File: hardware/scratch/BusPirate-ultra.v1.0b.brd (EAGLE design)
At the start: 100 x 50 mm, 177 parts, among them IC1 23LC1024, IC10 SN74LVC1T45DBV, IC11 SN74LVC1T45DBV, IC12 74LVC1G07DBV, IC13 SN74LVC1T45DBV, IC17 74LVC1G07DBV, IC18 SN74LVC1T45DBV, IC19 74LVC1G07DBV, IC2 23LC1024, IC20 SN74LVC1T45DBV, IC21 74LVC1G07DBV, IC22 SN74LVC1T45DBV, IC23 MCP1824_ADJ, IC24 74HCT4051, IC3 74AC573, IC4 74LVC1G07DBV, IC5 74LVC1G07DBV, IC6 74LVC1G07DBV, IC7 74LVC1G07DBV, IC8 SN74LVC1T45DBV, IC9 SN74LVC1T45DBV, J2 CON_HEADER_1X04, J4 CON_HEADER_1X10-RIGHT_ANGLED_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, Q1 DMMT3906W, U1 W25X40CL, U2 STM32F103ZX, U3 ICE40HX4K, U4 MCP6001, U5 MCP4442, U6 MCP4442, U7 MCP6001

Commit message: below are the changes in the schematic -remove extra pull-down resistor on VREGEN -BOOT0 and BOOT1 now connect directly to GND -change latch nets naming scheme -add divider resistors to sense voltage to Vout/Vref -renamed the control pins of the rest of the buffers -move UART to USART1 (PA9 and PA10) -connect digital pot to ARM's I2C1 (PB6 and PB7) with their pull-ups resistors, A0 and A1 wired to (PE5 and PE6) -all ADC Mux control lines are controlled only by FPGA -flip the order of latch connection of FPGA
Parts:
- added R52: 10K, dp_devices.v6:R603
- R4: device dp_devices:R603 -> dp_devices.v6:R603
- R7, R8: device rcl:R0603 -> resistor:R0603
- moved R8 273.5 mm to (-10.8, -231.8), turned to 0 degrees
- moved R7 266.4 mm to (-10.8, -226.7), turned to 0 degrees
- moved R49 241.1 mm to (-10.8, -237.5), turned to 0 degrees
- moved R4 35.1 mm to (8.89, 2.79), turned to 180 degrees
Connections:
- net ADC5 renamed MCU_ADC5
- net LAT_AUX0 renamed LAT3
- net LAT_AUX1 renamed LAT2
- net LAT_AUX2 renamed LAT1
- net LAT_AUX3 renamed LAT0
- net LAT_CLOCK renamed LAT6
- net LAT_CS renamed LAT4
- net LAT_MISO renamed LAT5
- net LAT_MOSI renamed LAT7
- removed net BOOT0: R8.1, U2.138
- removed net BOOT1: R7.1, U2.48
- removed net BUFDIR_AUX1: IC18.5, R35.2
- removed net BUFDIR_AUX2: IC20.5, R38.2
- removed net BUFDIR_AUX3: IC22.5, R41.2
- removed net BUFIO_AUX1: IC18.3
- removed net BUFIO_AUX2: IC20.3
- removed net BUFIO_AUX3: IC22.3
- removed net BUFOD_AUX1: IC17.2, R34.1
- removed net BUFOD_AUX2: IC19.2, R37.1
- removed net BUFOD_AUX3: IC21.2, R40.1
- removed net N$31: U5.11
- removed net N$33: U5.3
- removed net N$45: U2.102
- removed net N$46: U2.101
- removed net N$49: U5.4
- removed net N$50: U5.5
- removed net N$51: U6.11
- removed net N$55: U6.3
- removed net N$62: U6.4
- removed net N$63: U6.5
- new net BUFDIR5: IC18.5, R35.2, U3.88
- new net BUFDIR6: IC20.5, R38.2, U3.61
- new net BUFDIR7: IC22.5, R41.2, U3.64
- new net BUFIO5: IC18.3, U3.87
- new net BUFIO6: IC20.3, U3.60
- new net BUFIO7: IC22.3, U3.63
- new net BUFOD5: IC17.2, R34.1, U3.85
- new net BUFOD6: IC19.2, R37.1, U3.56
- new net BUFOD7: IC21.2, R40.1, U3.62
- new net MCU_ADC6: R7.2, R8.2, U2.36
- new net MCU_I2C_A0: U2.4, U5.3, U6.3
- new net MCU_I2C_A1: U2.5, U5.11, U6.11
- new net MCU_I2C_SCL: R49.1, U2.136, U5.4, U6.4
- new net MCU_I2C_SDA: R52.1, U2.137, U5.5, U6.5
- net 3V3: now also R49.2, R52.2
- net ADC_MUX_S0: no longer U2.87
- net ADC_MUX_S1: no longer U2.88
- net ADC_MUX_S2: no longer U2.89
- net BPIO0: now also IC3.9; no longer IC3.2
- net BPIO1: now also IC3.8; no longer IC3.3
- net BPIO2: now also IC3.7; no longer IC3.4
- net BPIO3: now also IC3.6; no longer IC3.5
- net BPIO4: now also IC3.5; no longer IC3.6
- net BPIO5: now also IC3.4; no longer IC3.7
- net BPIO6: now also IC3.3; no longer IC3.8
- net BPIO7: now also IC3.2; no longer IC3.9
- net GND: now also R8.1, U2.138, U2.48; no longer R49.2, R7.2, R8.2
- net N$29: now also U2.116; no longer U2.36
- net UART_RX: now also U2.102; no longer U2.137
- net UART_TX: now also U2.101; no longer U2.136
- net VREF/VOUT: now also R7.1
- net VREGEN: no longer R49.1
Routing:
- net BOOT1: track 39.3 -> 0.00 mm, vias 2 -> 0
- net 3V3: track 501.6 -> 482.6 mm
- net BOOT0: track 13.0 -> 0.00 mm
- net UART_TX: track 11.7 -> 0.00 mm
- net MCU_I2C_SCL: track 0.00 -> 11.7 mm
- net BPIO2: track 22.5 -> 33.5 mm
- net BPIO5: track 31.2 -> 20.2 mm
- net GND: track 19.3 -> 30.0 mm
- net UART_RX: track 8.41 -> 0.00 mm
- net MCU_I2C_SDA: track 0.00 -> 8.41 mm
- net BPIO7: track 19.3 -> 13.2 mm
- net BPIO0: track 20.2 -> 24.3 mm
- net BPIO6: track 13.1 -> 10.6 mm
- net VREGEN: track 85.8 -> 85.1 mm

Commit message: fix digital pots address lines voltage reg DAC buffer opamp (MCP6001), shorted the feedback, change R45 value to 100K, remove C62, added devider resistors R47(78.7K) and R46(50K), removed input resistor R48, add input cap initial change to small package (SC-70, 0402) IO-0 buffer
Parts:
- removed C62: 0.1uF, dp_devices.v6:C603
- removed R48: 1M, dp_devices.v6:R603
- added C53: (no value), dp_devices.v6:C603
- C39, C45: device rcl:C0603 -> rcl:C0402
- IC4: device 74xx-little-de:SOT23-5 -> dp_devices.v6:SC-70-5
- IC8: device dp_devices.v6:DBV-R-PDSO-G6 -> dp_devices.v6:SC-70-6
- R19, R24, R28: device rcl:R0603 -> rcl:R0402
- R45: value 330R -> 100K
- R46: value (none) -> 50K
- R47: value (none) -> 78.7K
- moved R28 1.55 mm to (81.7, 14.5), turned to 90 degrees
- moved C39 1.27 mm to (79.4, 17.1)
- moved R24 1.27 mm to (81.3, 12.1)
- moved R19 1.02 mm to (77.5, 12.1)
- moved C45 0.76 mm to (81.7, 17.8)
- moved IC8 0.76 mm to (79.4, 15.1)
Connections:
- removed net ADC3: U2.41
- removed net ADC4: U2.40
- removed net MCU_I2C_A0: U2.4, U5.3, U6.3
- removed net MCU_I2C_A1: U2.5, U5.11, U6.11
- removed net N$15: R46.2, R47.1, U4.3
- removed net VREG_PWM: R48.2
- new net VREG_DAC: C53.1, U2.40, U4.3
- net 3V3: now also U6.3
- net GND: now also C53.2, R46.2, U5.11, U5.3, U6.11; no longer C62.2, R47.2
- net N$12: now also R47.2; no longer U4.1
- net N$25: now also R47.1, U4.1; no longer C62.1, R48.1
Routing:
- net N$15: track 3.87 -> 0.00 mm
- net N$25: track 3.72 -> 0.00 mm
- net BPIO0: track 24.3 -> 21.1 mm
- net N$12: track 10.4 -> 9.35 mm
- net 3V3: track 482.6 -> 483.6 mm
- net BUFIO0: track 17.3 -> 18.0 mm
- net GND: vias 138 -> 136

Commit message: place 0R resistor on the feedback of vreg DAC buffer and placed an rc filter on the input. replace with 10uF cap on the adj vreg chip input. change buffer chip with an SC-70 packages and 0402 caps and resitors
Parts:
- added R48: (no value), dp_devices.v6:R603
- added R53: 0R, dp_devices.v6:R603
- C40, C41, C42, C43, C46, C47, C48, C49: device rcl:C0603 -> resistor:C0402
- C63: value 0.1uF -> 10uF
- IC10, IC11, IC13, IC18, IC20, IC22, IC9: device dp_devices.v6:DBV-R-PDSO-G6 -> dp_devices.v6:SC-70-6
- IC12, IC17, IC19, IC21, IC5, IC6, IC7: device 74xx-little-de:SOT23-5 -> dp_devices.v6:SC-70-5
- R19, R24, R28: device rcl:R0402 -> resistor:R0402
- R20, R21, R22, R23, R25, R26, R27, R29, R30, R31, R32, R33, R40: device rcl:R0603 -> resistor:R0402
- moved R41 122.7 mm to (64.1, 3.81), turned to 90 degrees
- moved C59 118.3 mm to (58.4, 7.62), turned to 90 degrees
- moved C60 117.9 mm to (64.1, 7.62), turned to 90 degrees
- moved R42 117.2 mm to (64.1, 1.27)
- moved IC22 113.1 mm to (61.0, 7.62), turned to 90 degrees
- moved R38 109.6 mm to (73.7, 3.81), turned to 90 degrees
- moved R40 108.0 mm to (58.4, 3.79), turned to 90 degrees
- moved R39 104.0 mm to (73.7, 1.91)
- moved C58 103.9 mm to (73.7, 7.62), turned to 90 degrees
- moved R35 103.7 mm to (83.2, 5.08)
- moved C57 103.5 mm to (66.7, 7.62), turned to 90 degrees
- moved IC21 103.4 mm to (61.0, 3.17)
- moved IC20 100.5 mm to (70.5, 7.62), turned to 90 degrees
- moved R36 97.7 mm to (83.2, 3.17)
- moved C56 97.1 mm to (83.2, 8.26)
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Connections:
- new net N$15: R53.1, U4.4
- new net N$31: C53.1, R48.2, U4.3
- net N$25: now also R53.2; no longer U4.4
- net VREG_DAC: now also R48.1; no longer C53.1, U4.3
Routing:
- net ADC1: track 57.3 -> 47.1 mm
- net BUFOD3: track 9.98 -> 18.0 mm
- net VREF/VOUT: track 173.7 -> 168.0 mm
- net BUFDIR2: track 21.6 -> 26.3 mm
- net BUFOD4: track 18.0 -> 14.4 mm
- net BUFDIR4: track 22.5 -> 25.3 mm
- net BPIO0: track 21.1 -> 18.4 mm
- net BPIO3: track 40.0 -> 37.5 mm
- net 3V3: track 483.6 -> 485.8 mm
- net BUFDIR1: track 10.4 -> 8.50 mm
- net BPIO1: track 28.0 -> 26.7 mm
- net BUFOD1: track 9.75 -> 8.92 mm
- net BUFDIR3: track 15.5 -> 16.2 mm
- net BUFOD2: track 15.1 -> 15.6 mm
- net GND: vias 136 -> 134

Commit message: latch's OE tied to gnd, move things around
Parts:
- C55, C56, C57, C58, C59, C60: device rcl:C0603 -> resistor:C0402
- IC10, IC11, IC13, IC18, IC20, IC22, IC8, IC9: device dp_devices.v6:SC-70-6 -> dp_devices.v6:SC-70-6_EXTENDED_PADS
- IC12, IC17, IC19, IC21, IC4, IC5, IC6, IC7: device dp_devices.v6:SC-70-5 -> dp_devices.v6:SC-70-5_EXTENDED_PADS
- R34, R35, R36, R37, R38, R39, R41, R42: device rcl:R0603 -> resistor:R0402
- moved R52 288.8 mm to (15.2, 44.5)
- moved R49 285.0 mm to (15.2, 46.4)
- moved R53 269.6 mm to (12.7, 10.2)
- moved R48 263.6 mm to (8.26, 10.2)
- moved C53 258.5 mm to (8.26, 8.89)
- moved R8 244.1 mm to (29.8, 8.89)
- moved R51 241.4 mm to (70.5, 4.45)
- moved R7 238.4 mm to (26.0, 8.89)
- moved C51 238.2 mm to (69.8, 6.35)
- moved C14 232.4 mm to (66.7, 6.35)
- moved C44 230.2 mm to (84.5, 46.4), turned to 180 degrees
- moved TP8 229.0 mm to (10.8, 36.2)
- moved D1 226.8 mm to (66.7, 4.45)
- moved TP7 226.5 mm to (10.8, 38.1)
- moved TP6 223.9 mm to (10.8, 40.0)
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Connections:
- removed net LAT_OE: IC3.1, U3.90
- net BPIO0: now also IC3.2; no longer IC3.9
- net BPIO1: now also IC3.3; no longer IC3.8
- net BPIO2: now also IC3.4; no longer IC3.7
- net BPIO3: now also IC3.5; no longer IC3.6
- net BPIO4: now also IC3.6; no longer IC3.5
- net BPIO5: now also IC3.7; no longer IC3.4
- net BPIO6: now also IC3.8; no longer IC3.3
- net BPIO7: now also IC3.9; no longer IC3.2
- net GND: now also IC3.1
- net LAT0: now also IC3.19; no longer IC3.12
- net LAT1: now also IC3.18; no longer IC3.13
- net LAT2: now also IC3.17; no longer IC3.14
- net LAT3: now also IC3.16; no longer IC3.15
- net LAT4: now also IC3.15; no longer IC3.16
- net LAT5: now also IC3.14; no longer IC3.17
- net LAT6: now also IC3.13; no longer IC3.18
- net LAT7: now also IC3.12; no longer IC3.19
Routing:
- net 3V3: track 485.8 -> 440.2 mm, vias 37 -> 29
- net BPIO2: track 33.5 -> 4.70 mm, vias 2 -> 0
- net BPIO3: track 37.5 -> 14.4 mm, vias 1 -> 0
- net BUFDIR2: track 26.3 -> 5.33 mm, vias 2 -> 0
- net LAT_OE: track 19.4 -> 0.00 mm, vias 2 -> 0
- net BUFOD0: track 22.4 -> 3.28 mm
- net VREF/VOUT: track 168.0 -> 149.3 mm, vias 9 -> 5
- net BPIO0: track 18.4 -> 0.00 mm, vias 1 -> 0
- net GND: track 30.0 -> 11.6 mm, vias 134 -> 100
- net BUFDIR0: track 22.1 -> 3.66 mm, vias 2 -> 0
- net BUFOD3: track 18.0 -> 0.00 mm
- net BUFIO0: track 18.4 -> 2.02 mm, vias 0 -> 1
- net BUFOD2: track 15.6 -> 0.00 mm
- net BUFIO4: track 17.7 -> 2.37 mm
- net BPIO1: track 26.7 -> 11.9 mm, vias 2 -> 0
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
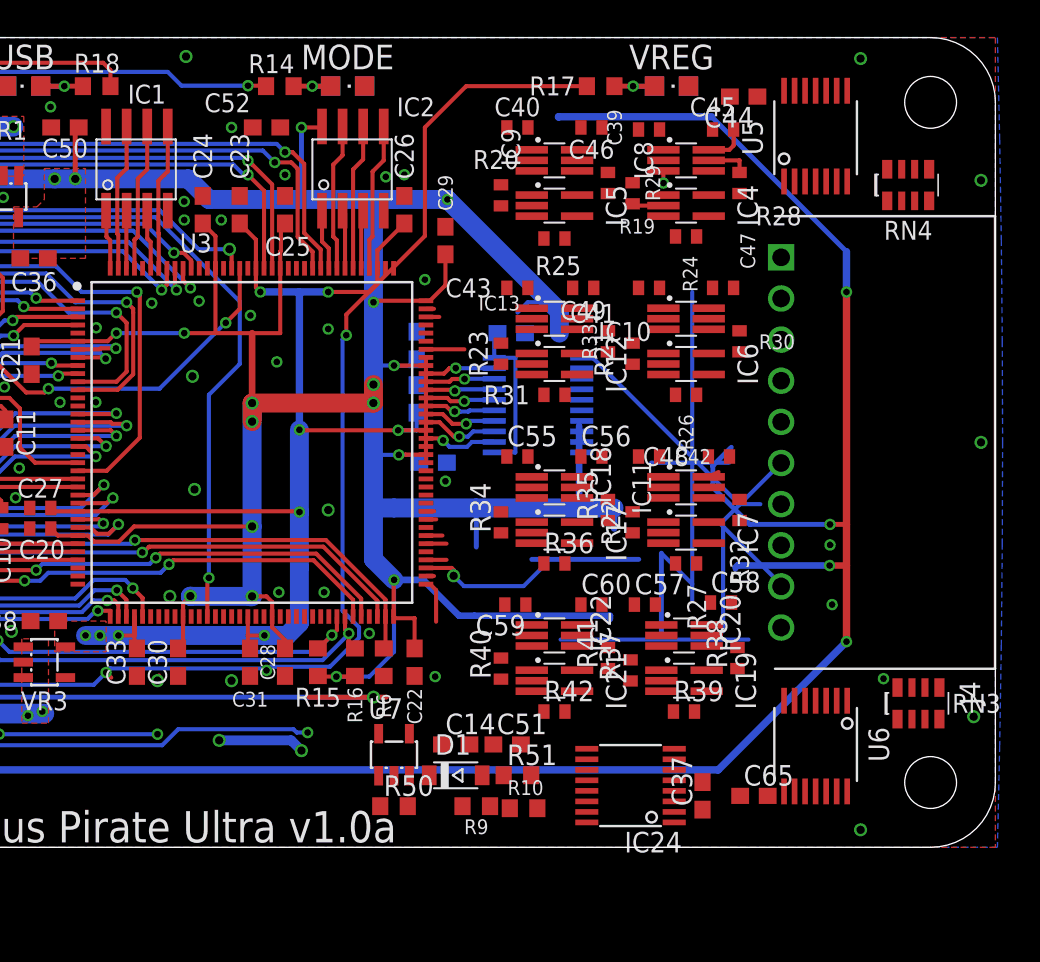
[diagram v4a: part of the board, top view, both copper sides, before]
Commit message: ADC mux chip 4051 Vcc connected to VUSB, digital pots (MCP4442) supply vdd connected to VUSB
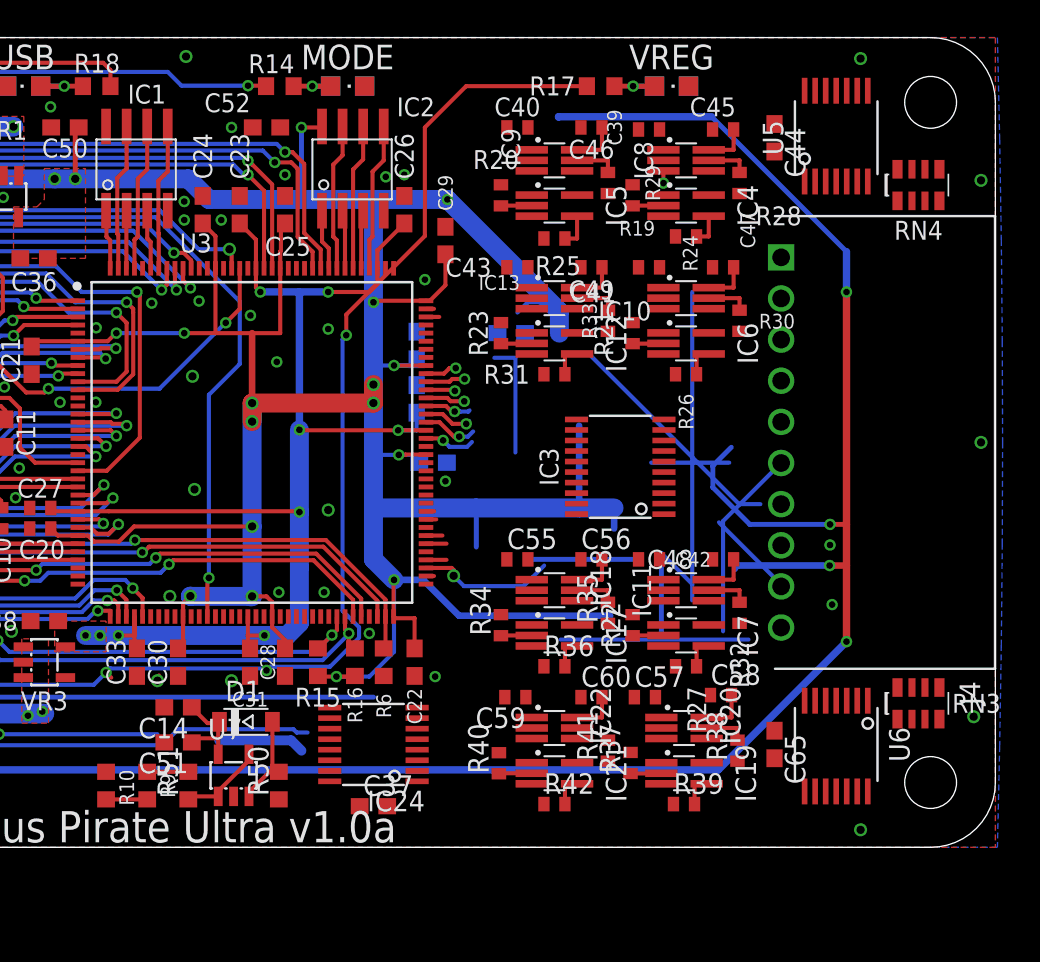
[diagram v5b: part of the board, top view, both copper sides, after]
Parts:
- moved R10 25.8 mm to (45.1, 3.81), turned to 270 degrees
- moved R9 20.4 mm to (47.6, 3.81), turned to 270 degrees
- moved C37 20.3 mm to (61.6, 2.54), turned to 0 degrees
- moved R51 20.3 mm to (50.2, 3.81), turned to 90 degrees
- moved C51 20.3 mm to (49.5, 6.48), turned to 180 degrees
- moved C14 17.3 mm to (49.5, 8.64), turned to 180 degrees
- moved IC24 16.1 mm to (61.6, 6.35)
- moved D1 13.4 mm to (53.7, 7.75)
- moved U7 9.99 mm to (53.0, 4.45)
- moved R50 7.22 mm to (55.8, 3.81), turned to 90 degrees
- moved C48 6.36 mm to (83.2, 17.8)
- moved IC11 6.35 mm to (80.9, 15.9)
- moved IC17 6.35 mm to (72.8, 13.1)
- moved IC18 6.35 mm to (72.8, 15.9)
- moved IC7 6.35 mm to (80.9, 13.1)
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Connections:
- net 3V3: no longer C37.1, C44.1, C65.1, IC24.16, U5.12, U6.12
- net VUSB: now also C37.1, C44.1, C65.1, IC24.16, U5.12, U6.12
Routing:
- net VREF/VOUT: track 149.3 -> 168.6 mm
- net N$32: track 0.00 -> 5.87 mm
- net VUSB: track 94.2 -> 100.0 mm
- net N$64: track 0.00 -> 5.31 mm
- net BUFOD4: track 6.29 -> 1.92 mm
- net 3V3: track 440.2 -> 437.3 mm
- net BUFDIR6: track 0.00 -> 2.65 mm
- net BUFDIR5: track 0.00 -> 2.65 mm
- net BUFDIR4: track 19.0 -> 21.7 mm
- net BUFDIR3: track 4.12 -> 6.77 mm
- net BUFDIR2: track 5.33 -> 7.98 mm
- net BUFDIR1: track 8.50 -> 11.1 mm
- net N$65: track 0.00 -> 2.54 mm
- net BUFIO4: track 2.37 -> 0.00 mm
- net LAT0: track 4.36 -> 1.99 mm
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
